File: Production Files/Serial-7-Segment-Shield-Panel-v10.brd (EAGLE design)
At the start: 59.7 x 53.3 mm, 32 parts, among them J1 AVR_SPI_PRG_6PTH, U1 ARDUINO_SHIELDLABEL

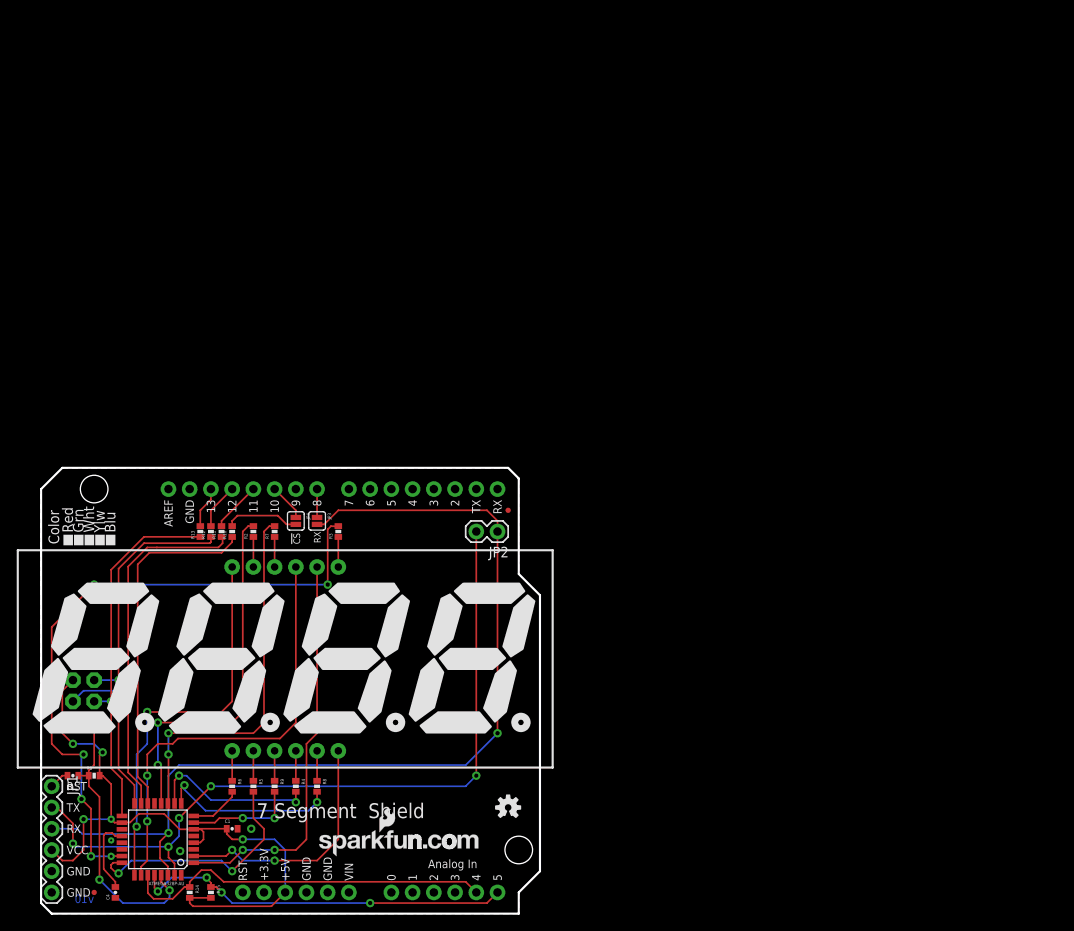
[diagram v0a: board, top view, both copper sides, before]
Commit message: v10 Production Ready files
Change version number on boards to v10
Created board panel for manufacture
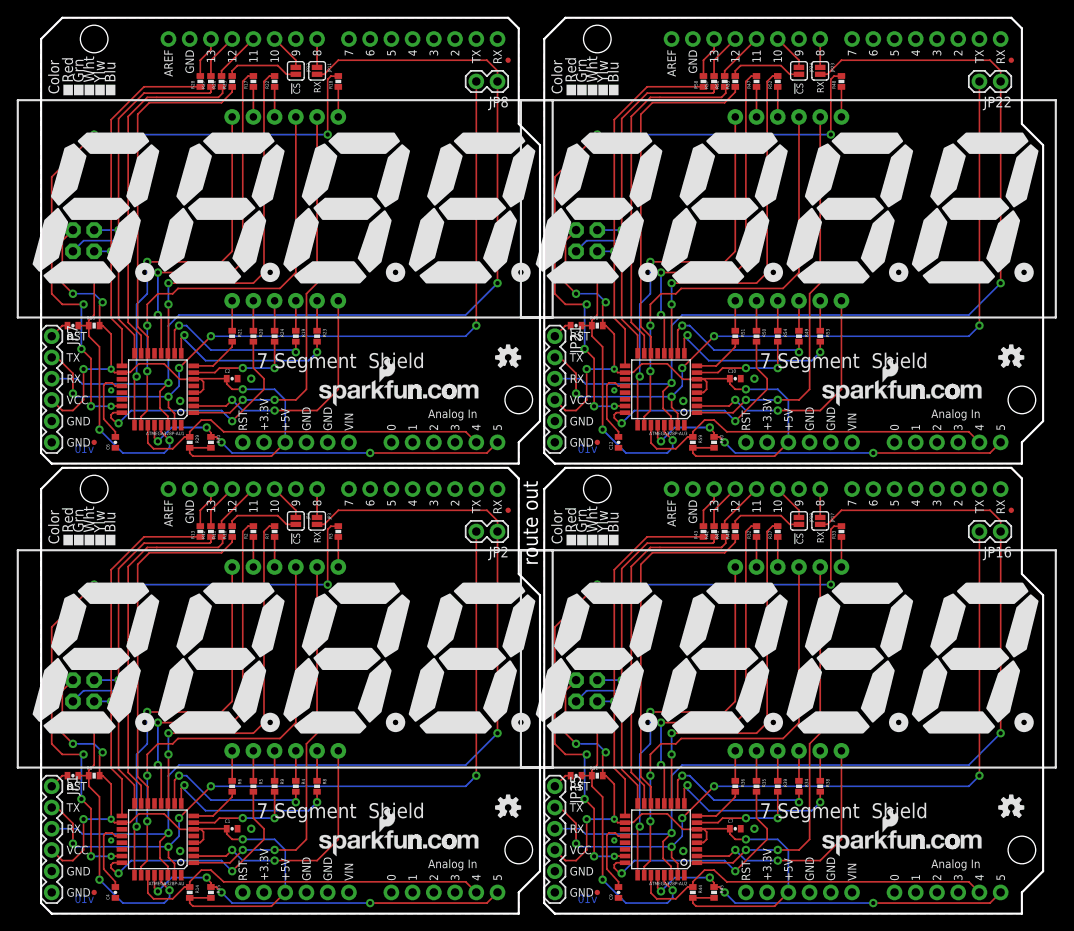
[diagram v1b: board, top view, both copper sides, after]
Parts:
- removed FRAME1: FRAME-LETTER, SparkFun-Aesthetics:CREATIVE_COMMONS
- added ATMEGA328P-AU1, ATMEGA328P-AU2, ATMEGA328P-AU3: ATMEGA328P-AU, SparkFun:TQFP32-08
- added C10, C2, C7: 0.1uF, SparkFun:0402-CAP
- added C11, C12, C5, C6, C8, C9: 0.1uF, SparkFun-Passives:0402-CAP
- added J2, J3, J4: AVR_SPI_PRG_6PTH, SparkFun-Connectors:2X3
- added JP11, JP12, JP17, JP18, JP23, JP24: NC, SparkFun-Passives:SJ_2S
- added JP13, JP14, JP19, JP20, JP5, JP6: FIDUCIALUFIDUCIAL, SparkFun:MICRO-FIDUCIAL
- added JP15, JP21, JP7: (no value), SparkFun-Connectors:1X06
- added JP16, JP22, JP8: (no value), SparkFun-Connectors:1X02
- added LOGO3, LOGO4, LOGO5, LOGO6, LOGO7, LOGO8: LOGO-SFENEW, SparkFun-Aesthetics:SFE-NEW-WEBLOGO
- added R16, R29, R30, R31, R44, R45, R46, R59, R60: 10k, SparkFun:0402-RES
- added R17, R18, R19, R20, R21, R22, R23, R24, R32, R33, R34, R35, R36, R37, R38, R39, R47, R48, R49, R50, R51, R52, R53, R54: 100, SparkFun:0402-RES
- added R25, R26, R27, R28, R40, R41, R42, R43, R55, R56, R57, R58: 1k, SparkFun:0402-RES
- added U$2, U$5, U$7: OSHW-LOGOS, SparkFun-Aesthetics:OSHW-LOGO-S
- added U$3, U$6, U$8: 7-SEGMENT-4DIGIT-COUNTERPTH, SparkFun-Displays:7-SEGMENT-4DIGIT-COUNTER
- added U2, U3, U4: ARDUINO_SHIELDLABEL, SparkFun-Boards:DUEMILANOVE_SHIELD
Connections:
- new net !SS1: ATMEGA328P-AU1.14, R25.1
- new net !SS2: ATMEGA328P-AU2.14, R40.1
- new net !SS3: ATMEGA328P-AU3.14, R55.1
- new net A1: ATMEGA328P-AU1.12, R17.2
- new net A2: ATMEGA328P-AU2.12, R32.2
- new net A3: ATMEGA328P-AU3.12, R47.2
- new net ADC1: ATMEGA328P-AU1.19
- new net ADC2: ATMEGA328P-AU1.22
- new net ADC3: ATMEGA328P-AU2.19
- new net ADC4: ATMEGA328P-AU2.22
- new net ADC5: ATMEGA328P-AU3.19
- new net ADC8: ATMEGA328P-AU3.22
- new net B1: ATMEGA328P-AU1.23, R18.2
- new net B2: ATMEGA328P-AU2.23, R33.2
- new net B3: ATMEGA328P-AU3.23, R48.2
- new net C1: ATMEGA328P-AU1.10, R19.2
- new net C2: ATMEGA328P-AU2.10, R34.2
- new net C3: ATMEGA328P-AU3.10, R49.2
- new net D1: ATMEGA328P-AU1.24, R20.2
- new net D2: ATMEGA328P-AU2.24, R35.2
- new net D3: ATMEGA328P-AU3.24, R50.2
- new net DIG10: ATMEGA328P-AU2.1, U$6.8
- new net DIG11: ATMEGA328P-AU2.26, U$6.9
- new net DIG12: ATMEGA328P-AU2.25, U$6.12
- new net DIG13: ATMEGA328P-AU3.2, U$8.6
- new net DIG14: ATMEGA328P-AU3.1, U$8.8
- new net DIG15: ATMEGA328P-AU3.26, U$8.9
- new net DIG16: ATMEGA328P-AU3.25, U$8.12
- new net DIG5: ATMEGA328P-AU1.2, U$3.6
- new net DIG6: ATMEGA328P-AU1.1, U$3.8
- new net DIG7: ATMEGA328P-AU1.26, U$3.9
- new net DIG8: ATMEGA328P-AU1.25, U$3.12
- new net DIG9: ATMEGA328P-AU2.2, U$6.6
- new net DP1: ATMEGA328P-AU1.7, R24.2
- new net DP2: ATMEGA328P-AU2.7, R39.2
- new net DP3: ATMEGA328P-AU3.7, R54.2
- new net E1: ATMEGA328P-AU1.8, R21.2
- new net E2: ATMEGA328P-AU2.8, R36.2
- new net E3: ATMEGA328P-AU3.8, R51.2
- new net F1: ATMEGA328P-AU1.11, R22.2
- new net F2: ATMEGA328P-AU2.11, R37.2
- new net F3: ATMEGA328P-AU3.11, R52.2
- new net G1: ATMEGA328P-AU1.9, R23.2
- new net G2: ATMEGA328P-AU2.9, R38.2
- new net G3: ATMEGA328P-AU3.9, R53.2
- new net GND1: ATMEGA328P-AU1.21, ATMEGA328P-AU1.3, ATMEGA328P-AU1.5, C2.2, C6.1, J2.6, JP7.5, JP7.6, U2.GND@0, U2.GND@1, U2.GND@2
- new net GND2: ATMEGA328P-AU2.21, ATMEGA328P-AU2.3, ATMEGA328P-AU2.5, C7.2, C9.1, J3.6, JP15.5, JP15.6, U3.GND@0, U3.GND@1, U3.GND@2
- new net GND3: ATMEGA328P-AU3.21, ATMEGA328P-AU3.3, ATMEGA328P-AU3.5, C10.2, C12.1, J4.6, JP21.5, JP21.6, U4.GND@0, U4.GND@1, U4.GND@2
- new net MISO1: ATMEGA328P-AU1.16, J2.1, R27.1
- new net MISO2: ATMEGA328P-AU2.16, J3.1, R42.1
- new net MISO3: ATMEGA328P-AU3.16, J4.1, R57.1
- new net MOSI1: ATMEGA328P-AU1.15, J2.4, R26.1
- new net MOSI2: ATMEGA328P-AU2.15, J3.4, R41.1
- new net MOSI3: ATMEGA328P-AU3.15, J4.4, R56.1
- new net N$10: R17.1, U$3.11
- new net N$20: R18.1, U$3.7
- new net N$21: R19.1, U$3.4
- new net N$22: R20.1, U$3.2
- new net N$23: R21.1, U$3.1
- new net N$24: R22.1, U$3.10
- new net N$25: R23.1, U$3.5
- new net N$26: R24.1, U$3.3
- new net N$27: R28.2, U2.D13
- new net N$28: R27.2, U2.D12
- new net N$29: R26.2, U2.D11
- new net N$30: JP12.2, R25.2
- new net N$31: JP12.1, U2.D10
- new net N$32: JP11.1, U2.D8
- new net N$33: C8.2, JP15.1
- new net N$34: ATMEGA328P-AU2.20, C9.2
- new net N$35: R32.1, U$6.11
- new net N$36: R33.1, U$6.7
- new net N$37: R34.1, U$6.4
- new net N$38: R35.1, U$6.2
- new net N$39: R36.1, U$6.1
- new net N$40: R37.1, U$6.10
- new net N$41: R38.1, U$6.5
- new net N$42: R39.1, U$6.3
- new net N$43: R43.2, U3.D13
- new net N$44: R42.2, U3.D12
- new net N$45: R41.2, U3.D11
- new net N$46: JP18.2, R40.2
- new net N$47: JP18.1, U3.D10
- new net N$48: JP17.1, U3.D8
- new net N$49: C11.2, JP21.1
- new net N$50: ATMEGA328P-AU3.20, C12.2
- new net N$51: R47.1, U$8.11
- new net N$52: R48.1, U$8.7
- new net N$53: R49.1, U$8.4
- new net N$54: R50.1, U$8.2
- new net N$55: R51.1, U$8.1
- new net N$56: R52.1, U$8.10
- new net N$57: R53.1, U$8.5
- new net N$58: R54.1, U$8.3
- new net N$59: R58.2, U4.D13
- new net N$60: R57.2, U4.D12
- new net N$61: R56.2, U4.D11
- new net N$62: JP24.2, R55.2
- new net N$63: JP24.1, U4.D10
- new net N$64: JP23.1, U4.D8
- new net N$8: C5.2, JP7.1
- new net N$9: ATMEGA328P-AU1.20, C6.2
- new net RESET1: ATMEGA328P-AU1.29, C5.1, J2.5, R16.1
- new net RESET2: ATMEGA328P-AU2.29, C8.1, J3.5, R31.1
- new net RESET3: ATMEGA328P-AU3.29, C11.1, J4.5, R46.1
- new net RX1: ATMEGA328P-AU1.30, JP11.2, JP7.3, JP8.1
- new net RX2: ATMEGA328P-AU2.30, JP15.3, JP16.1, JP17.2
- new net RX3: ATMEGA328P-AU3.30, JP21.3, JP22.1, JP23.2
- new net SCK1: ATMEGA328P-AU1.17, J2.3, R28.1
- new net SCK2: ATMEGA328P-AU2.17, J3.3, R43.1
- new net SCK3: ATMEGA328P-AU3.17, J4.3, R58.1
- new net SCL1: ATMEGA328P-AU1.28, R30.1, U2.A5
- new net SCL2: ATMEGA328P-AU2.28, R45.1, U3.A5
- new net SCL3: ATMEGA328P-AU3.28, R60.1, U4.A5
- new net SDA1: ATMEGA328P-AU1.27, R29.1, U2.A4
- new net SDA2: ATMEGA328P-AU2.27, R44.1, U3.A4
- new net SDA3: ATMEGA328P-AU3.27, R59.1, U4.A4
- new net TX1: ATMEGA328P-AU1.31, JP7.2, JP8.2
- new net TX2: ATMEGA328P-AU2.31, JP15.2, JP16.2
- new net TX3: ATMEGA328P-AU3.31, JP21.2, JP22.2
- new net VCC1: ATMEGA328P-AU1.18, ATMEGA328P-AU1.4, ATMEGA328P-AU1.6, C2.1, J2.2, JP7.4, R16.2, R29.2, R30.2, U2.5V
- new net VCC2: ATMEGA328P-AU2.18, ATMEGA328P-AU2.4, ATMEGA328P-AU2.6, C7.1, J3.2, JP15.4, R31.2, R44.2, R45.2, U3.5V
- new net VCC3: ATMEGA328P-AU3.18, ATMEGA328P-AU3.4, ATMEGA328P-AU3.6, C10.1, J4.2, JP21.4, R46.2, R59.2, R60.2, U4.5V
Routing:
- net RX3: track 0.00 -> 116.7 mm, vias 0 -> 2
- net RX2: track 0.00 -> 116.7 mm, vias 0 -> 2
- net RX1: track 0.00 -> 116.7 mm, vias 0 -> 2
- net TX3: track 0.00 -> 91.9 mm, vias 0 -> 5
- net TX2: track 0.00 -> 91.9 mm, vias 0 -> 5
- net TX1: track 0.00 -> 91.9 mm, vias 0 -> 5
- net VCC2: track 0.00 -> 81.1 mm, vias 0 -> 5
- net VCC1: track 0.00 -> 81.1 mm, vias 0 -> 5
- net VCC3: track 0.00 -> 81.1 mm, vias 0 -> 5
- net B3: track 0.00 -> 78.0 mm, vias 0 -> 6
- net B2: track 0.00 -> 78.0 mm, vias 0 -> 6
- net B1: track 0.00 -> 78.0 mm, vias 0 -> 6
- net DIG7: track 0.00 -> 52.7 mm, vias 0 -> 2
- net DIG15: track 0.00 -> 52.7 mm, vias 0 -> 2
- net DIG11: track 0.00 -> 52.7 mm, vias 0 -> 2
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- added copper zone on layer 1, net GND1
- added copper zone on layer 16, net GND1
- added copper zone on layer 1, net GND2
- added copper zone on layer 16, net GND2
- added copper zone on layer 1, net GND3
- added copper zone on layer 16, net GND3
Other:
- board size 59.7 x 53.3 mm -> 119.9 x 107.2 mm
- board text added: "route out"
- board text removed: "Jordan McConnell"
